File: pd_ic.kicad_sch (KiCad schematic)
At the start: 19 parts, among them J11 Conn_01x02, J18 USB_C_Receptacle_USB2.0_16P, Q1 SiS443DN, U13 CYPD3175-24LQXQ, U17 TVS0500DRV

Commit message: lcsc again
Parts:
- C65, C68, C79: LCSC (none) -> C29266
- C80, C81: LCSC (none) -> C114397
- R44: LCSC (none) -> C60491
- R45: LCSC (none) -> C114763
- R46: LCSC (none) -> C137947
- R47: LCSC (none) -> C2903482
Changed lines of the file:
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@@
+			)
+		)
+		(property "LCSC" "C29266"
+			(at 74.93 73.66 0)
+			(effects
+				(font
+					(size 1.27 1.27)
+				)
+				(hide yes)
 			)
 		)
@@
 			)
 		)
+		(property "LCSC" "C29266"
+			(at 87.63 78.74 0)
+			(effects
+				(font
+					(size 1.27 1.27)
+				)
+				(hide yes)
+			)
+		)
 		(pin "2"
 		)
@@
 			)
 		)
+		(property "LCSC" "C137947"
+			(at 119.38 86.36 90)
+			(effects
+				(font
+					(size 1.27 1.27)
+				)
+				(hide yes)
+			)
+		)
 		(pin "2"
 		)
@@
 			)
 		)
+		(property "LCSC" "C114763"
+			(at 125.73 80.01 0)
+			(effects
+				(font
+					(size 1.27 1.27)
+				)
+				(hide yes)
+			)
+		)
 		(pin "2"
 		)
@@
 			)
 		)
+		(property "LCSC" "C114397"
+			(at 200.66 85.09 0)
+			(effects
+				(font
+					(size 1.27 1.27)
+				)
+				(hide yes)
+			)
+		)
 		(pin "1"
 		)
@@
 		)
 		(property "Description" "Resistor"
+			(at 152.4 59.69 0)
+			(effects
+				(font
+					(size 1.27 1.27)
+				)
+				(hide yes)
+			)
+		)
+		(property "LCSC" "C60491"
 			(at 152.4 59.69 0)
 			(effects
@@
 			)
 		)
+		(property "LCSC" "C2903482"
+			(at 161.29 142.24 90)
+			(effects
+				(font
+					(size 1.27 1.27)
+				)
+				(hide yes)
+			)
+		)
 		(pin "2"
 		)
@@
 			)
 		)
+		(property "LCSC" "C114397"
+			(at 191.77 87.63 0)
+			(effects
+				(font
+					(size 1.27 1.27)
+				)
+				(hide yes)
+			)
+		)
 		(pin "1"
 		)
@@
 			(at 143.51 71.12 0)
 			(effects
+				(font
+					(size 1.27 1.27)
+				)
+				(hide yes)
+			)
+		)
+		(property "LCSC" "C29266"
+			(at 143.51 71.12 0)
+			(effects

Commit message: standardised components, removing mixed values
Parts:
- C65, C68, C79: LCSC C29266 -> C52923
- C71, C78: LCSC C1525 -> C307331
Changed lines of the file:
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@@
 			)
 		)
-		(property "LCSC" "C29266"
+		(property "LCSC" "C52923"
 			(at 74.93 73.66 0)
 			(effects
@@
 			)
 		)
-		(property "LCSC" "C1525"
+		(property "LCSC" "C307331"
 			(at 99.06 96.52 0)
 			(effects
@@
 			)
 		)
-		(property "LCSC" "C29266"
+		(property "LCSC" "C52923"
 			(at 87.63 78.74 0)
 			(effects
@@
 			)
 		)
-		(property "LCSC" "C29266"
+		(property "LCSC" "C52923"
 			(at 143.51 71.12 0)
 			(effects
@@
 			)
 		)
-		(property "LCSC" "C1525"
+		(property "LCSC" "C307331"
 			(at 64.77 73.66 0)
 			(effects

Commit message: more lcsc
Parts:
- J11: LCSC (none) -> C52016390
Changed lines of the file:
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@@
+			)
+		)
+		(property "LCSC" "C52016390"
+			(at 121.92 99.06 0)
+			(effects
+				(font
+					(size 1.27 1.27)
+				)
+				(hide yes)
 			)
 		)

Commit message: ALL LCSC PARTS DONE
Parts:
- J18: LCSC (none) -> C3025063
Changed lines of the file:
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@@
+			)
+		)
+		(property "LCSC" "C3025063"
+			(at 232.41 113.03 0)
+			(effects
+				(font
+					(size 1.27 1.27)
+				)
+				(hide yes)
 			)
 		)

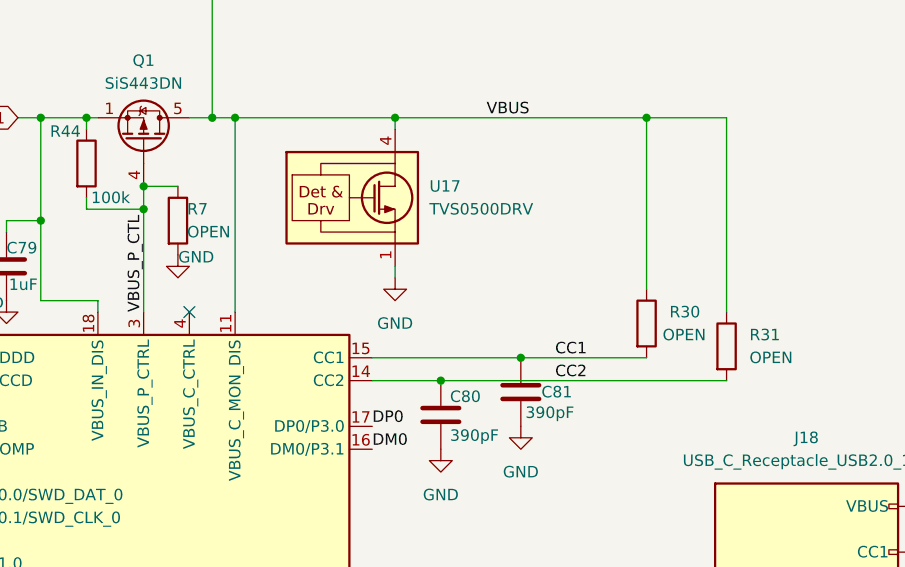
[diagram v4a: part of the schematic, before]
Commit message: Fixed errors with open resistors and led
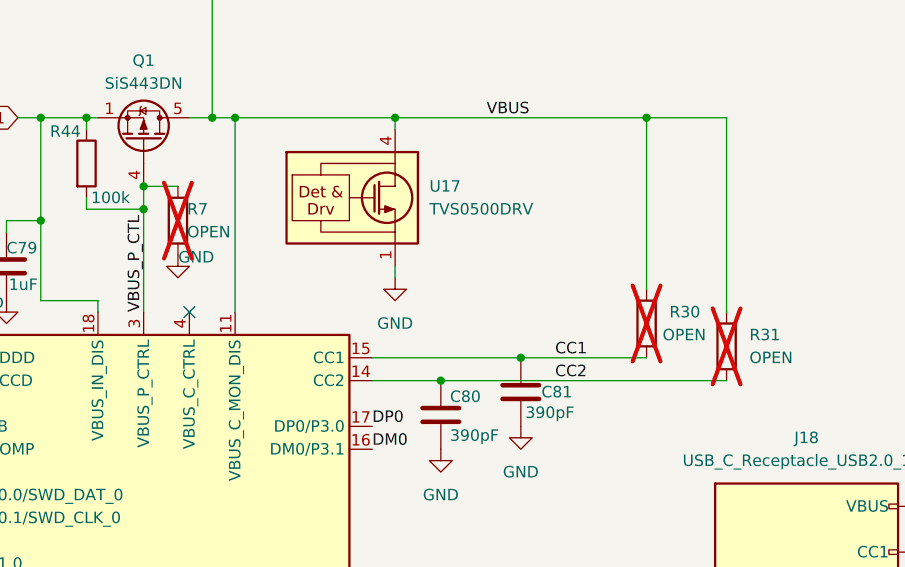
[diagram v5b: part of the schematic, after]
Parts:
- R30, R31, R7: now not fitted; now left out of the parts list
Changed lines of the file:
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@@
 		(unit 1)
 		(exclude_from_sim no)
-		(in_bom yes)
-		(on_board yes)
-		(dnp no)
+		(in_bom no)
+		(on_board yes)
+		(dnp yes)
 		(fields_autoplaced yes)
 		(property "Reference" "R31"
@@
 		(unit 1)
 		(exclude_from_sim no)
-		(in_bom yes)
-		(on_board yes)
-		(dnp no)
+		(in_bom no)
+		(on_board yes)
+		(dnp yes)
 		(property "Reference" "R7"
 			(at 163.576 64.77 0)
@@
 		(unit 1)
 		(exclude_from_sim no)
-		(in_bom yes)
-		(on_board yes)
-		(dnp no)
+		(in_bom no)
+		(on_board yes)
+		(dnp yes)
 		(property "Reference" "R30"
 			(at 217.17 76.1999 0)

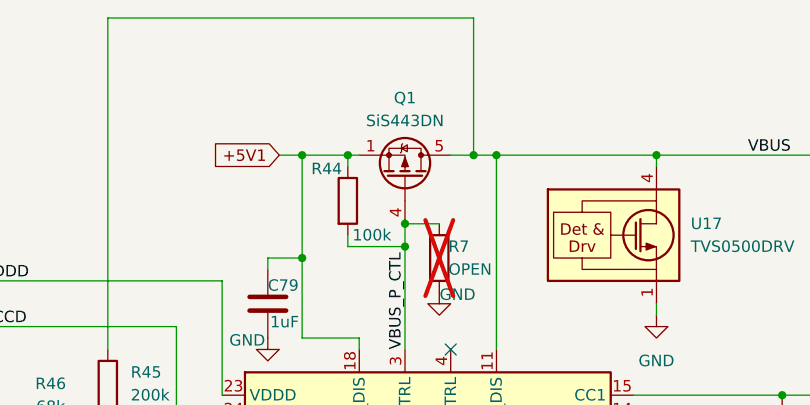
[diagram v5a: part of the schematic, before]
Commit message: changed mosfet lcsc part
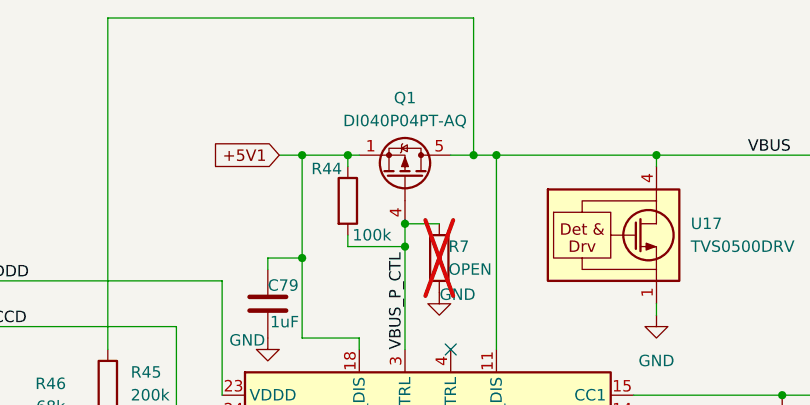
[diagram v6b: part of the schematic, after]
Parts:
- Q1: value SiS443DN -> DI040P04PT-AQ; LCSC C142539 -> C6934675
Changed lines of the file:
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@@
 			)
 		)
-		(property "Value" "SiS443DN"
+		(property "Value" "DI040P04PT-AQ"
 			(at 158.75 50.8 90)
 			(effects
@@
 			)
 		)
-		(property "LCSC" "C142539"
+		(property "LCSC" "C6934675"
 			(at 158.75 57.15 90)
 			(effects
